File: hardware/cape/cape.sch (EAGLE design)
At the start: 156 parts, among them IC1 AD8422BRMZ, IC10 DAC8562_DGS_10, IC11 CAT24C256WI-GT3, IC12 LM27762DSSR, IC13 BQ25505, IC14 SN74LV4T125PWR, IC15 LMP7701MF, IC16 TXB0304RUTR, IC2 OPA2388DGK8_L, IC3 AD8422BRMZ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

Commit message: hardware: fixed wrong part number for constant supply LDO
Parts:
- IC8: value TPS73125DBVR -> TPS73101DBVR; device mylib:TPS73125DBVR -> shepherd:TPS73101DBVR
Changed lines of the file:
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@@
 <?xml version="1.0" encoding="utf-8"?>
 <!DOCTYPE eagle SYSTEM "eagle.dtd">
-<eagle version="9.3.2">
+<eagle version="9.4.2">
 <drawing>
 <settings>
@@
 <part name="C35" library="mylib" deviceset="C_SMD" device="0603" package3d_urn="urn:adsk.eagle:package:4925888/1" value="1u"/>
 <part name="R31" library="mylib" deviceset="R_SMD" device="0402" package3d_urn="urn:adsk.eagle:package:4924763/1" value="10k"/>
-<part name="IC8" library="mylib" deviceset="TPS73125DBVR" device=""/>
+<part name="IC8" library="shepherd" deviceset="TPS73101DBVR" device=""/>
 <part name="D2" library="mylib" deviceset="BAT43WS-HE3" device="SOD-323" package3d_urn="urn:adsk.eagle:package:6206822/1"/>
 <part name="R26" library="mylib" deviceset="R_SMD" device="0402" package3d_urn="urn:adsk.eagle:package:4924763/1" value="30k"/>

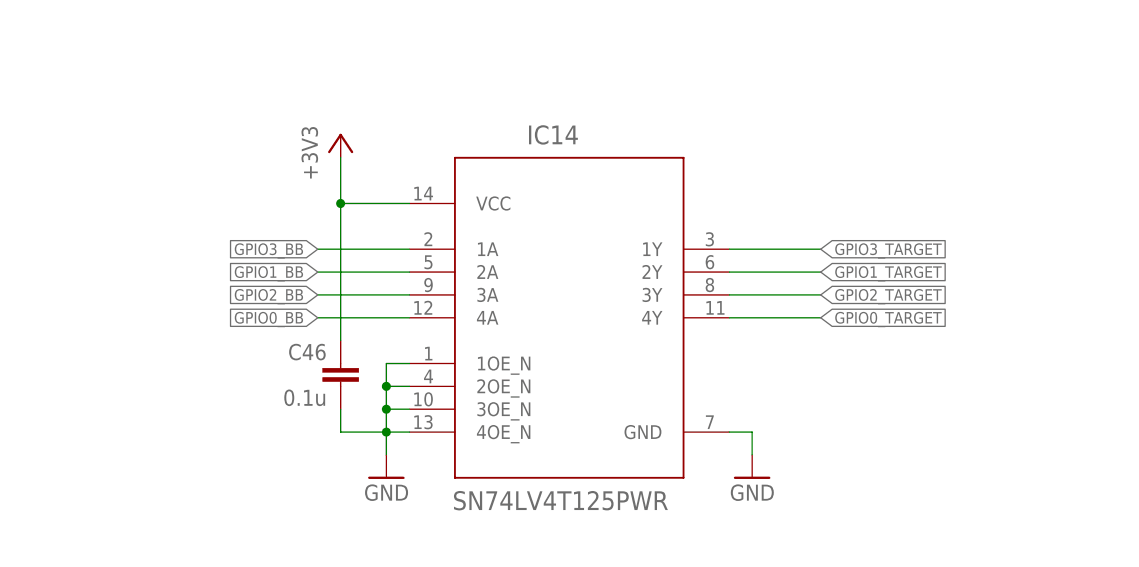
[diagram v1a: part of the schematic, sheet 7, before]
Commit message: hardware: fixed direction of level-converter
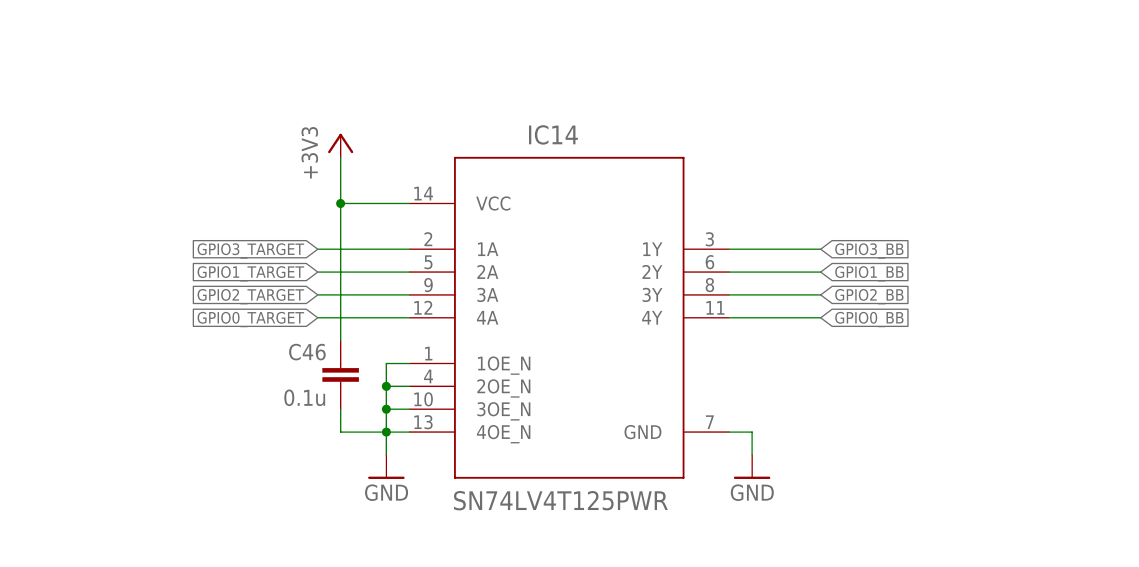
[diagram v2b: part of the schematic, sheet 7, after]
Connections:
- net GPIO0_BB: now also IC14.4Y; no longer IC14.4A
- net GPIO0_TARGET: now also IC14.4A; no longer IC14.4Y
- net GPIO1_BB: now also IC14.2Y; no longer IC14.2A
- net GPIO1_TARGET: now also IC14.2A; no longer IC14.2Y
- net GPIO2_BB: now also IC14.3Y; no longer IC14.3A
- net GPIO2_TARGET: now also IC14.3A; no longer IC14.3Y
- net GPIO3_BB: now also IC14.1Y; no longer IC14.1A
- net GPIO3_TARGET: now also IC14.1A; no longer IC14.1Y
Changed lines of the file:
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@@
 </segment>
 </net>
-<net name="GPIO3_BB" class="0">
+<net name="GPIO0_TARGET" class="0">
+<segment>
+<wire x1="53.34" y1="139.7" x2="43.18" y2="139.7" width="0.1524" layer="91"/>
+<label x="43.18" y="139.7" size="1.27" layer="95" rot="R180" xref="yes"/>
+<pinref part="IC14" gate="A" pin="4A"/>
+</segment>
+</net>
+<net name="GPIO1_TARGET" class="0">
+<segment>
+<wire x1="53.34" y1="144.78" x2="43.18" y2="144.78" width="0.1524" layer="91"/>
+<label x="43.18" y="144.78" size="1.27" layer="95" rot="R180" xref="yes"/>
+<pinref part="IC14" gate="A" pin="2A"/>
+</segment>
+</net>
+<net name="GPIO2_TARGET" class="0">
+<segment>
+<wire x1="53.34" y1="142.24" x2="43.18" y2="142.24" width="0.1524" layer="91"/>
+<label x="43.18" y="142.24" size="1.27" layer="95" rot="R180" xref="yes"/>
+<pinref part="IC14" gate="A" pin="3A"/>
+</segment>
+</net>
+<net name="GPIO3_TARGET" class="0">
 <segment>
 <wire x1="53.34" y1="147.32" x2="43.18" y2="147.32" width="0.1524" layer="91"/>
 <label x="43.18" y="147.32" size="1.27" layer="95" rot="R180" xref="yes"/>
 <pinref part="IC14" gate="A" pin="1A"/>
-</segment>
-</net>
-<net name="GPIO0_TARGET" class="0">
-<segment>
-<wire x1="88.9" y1="139.7" x2="99.06" y2="139.7" width="0.1524" layer="91"/>
-<label x="99.06" y="139.7" size="1.27" layer="95" xref="yes"/>
-<pinref part="IC14" gate="A" pin="4Y"/>
-</segment>
-</net>
-<net name="GPIO1_TARGET" class="0">
-<segment>
-<wire x1="88.9" y1="144.78" x2="99.06" y2="144.78" width="0.1524" layer="91"/>
-<label x="99.06" y="144.78" size="1.27" layer="95" xref="yes"/>
-<pinref part="IC14" gate="A" pin="2Y"/>
-</segment>
-</net>
-<net name="GPIO2_TARGET" class="0">
-<segment>
-<wire x1="88.9" y1="142.24" x2="99.06" y2="142.24" width="0.1524" layer="91"/>
-<label x="99.06" y="142.24" size="1.27" layer="95" xref="yes"/>
-<pinref part="IC14" gate="A" pin="3Y"/>
-</segment>
-</net>
-<net name="GPIO3_TARGET" class="0">
-<segment>
-<wire x1="88.9" y1="147.32" x2="99.06" y2="147.32" width="0.1524" layer="91"/>
-<label x="99.06" y="147.32" size="1.27" layer="95" xref="yes"/>
-<pinref part="IC14" gate="A" pin="1Y"/>
 </segment>
 </net>
@@
 <wire x1="86.36" y1="50.8" x2="104.14" y2="50.8" width="0.1524" layer="91"/>
 <junction x="104.14" y="50.8"/>
-</segment>
-</net>
-<net name="GPIO2_BB" class="0">
-<segment>
-<wire x1="53.34" y1="142.24" x2="43.18" y2="142.24" width="0.1524" layer="91"/>
-<label x="43.18" y="142.24" size="1.27" layer="95" rot="R180" xref="yes"/>
-<pinref part="IC14" gate="A" pin="3A"/>
 </segment>
 </net>
@@
 </segment>
 </net>
-<net name="GPIO0_BB" class="0">
+<net name="GPIO3_BB" class="0">
 <segment>
-<wire x1="53.34" y1="139.7" x2="43.18" y2="139.7" width="0.1524" layer="91"/>
-<label x="43.18" y="139.7" size="1.27" layer="95" rot="R180" xref="yes"/>
-<pinref part="IC14" gate="A" pin="4A"/>
+<wire x1="88.9" y1="147.32" x2="99.06" y2="147.32" width="0.1524" layer="91"/>
+<label x="99.06" y="147.32" size="1.27" layer="95" xref="yes"/>
+<pinref part="IC14" gate="A" pin="1Y"/>
 </segment>
 </net>
 <net name="GPIO1_BB" class="0">
 <segment>
-<wire x1="53.34" y1="144.78" x2="43.18" y2="144.78" width="0.1524" layer="91"/>
-<label x="43.18" y="144.78" size="1.27" layer="95" rot="R180" xref="yes"/>
-<pinref part="IC14" gate="A" pin="2A"/>
+<wire x1="88.9" y1="144.78" x2="99.06" y2="144.78" width="0.1524" layer="91"/>
+<label x="99.06" y="144.78" size="1.27" layer="95" xref="yes"/>
+<pinref part="IC14" gate="A" pin="2Y"/>
 </segment>
 </net>
+<net name="GPIO2_BB" class="0">
+<segment>
+<wire x1="88.9" y1="142.24" x2="99.06" y2="142.24" width="0.1524" layer="91"/>
+<label x="99.06" y="142.24" size="1.27" layer="95" xref="yes"/>
+<pinref part="IC14" gate="A" pin="3Y"/>
+</segment>
+</net>
+<net name="GPIO0_BB" class="0">
+<segment>
+<wire x1="88.9" y1="139.7" x2="99.06" y2="139.7" width="0.1524" layer="91"/>
+<label x="99.06" y="139.7" size="1.27" layer="95" xref="yes"/>
+<pinref part="IC14" gate="A" pin="4Y"/>
+</segment>
+</net>

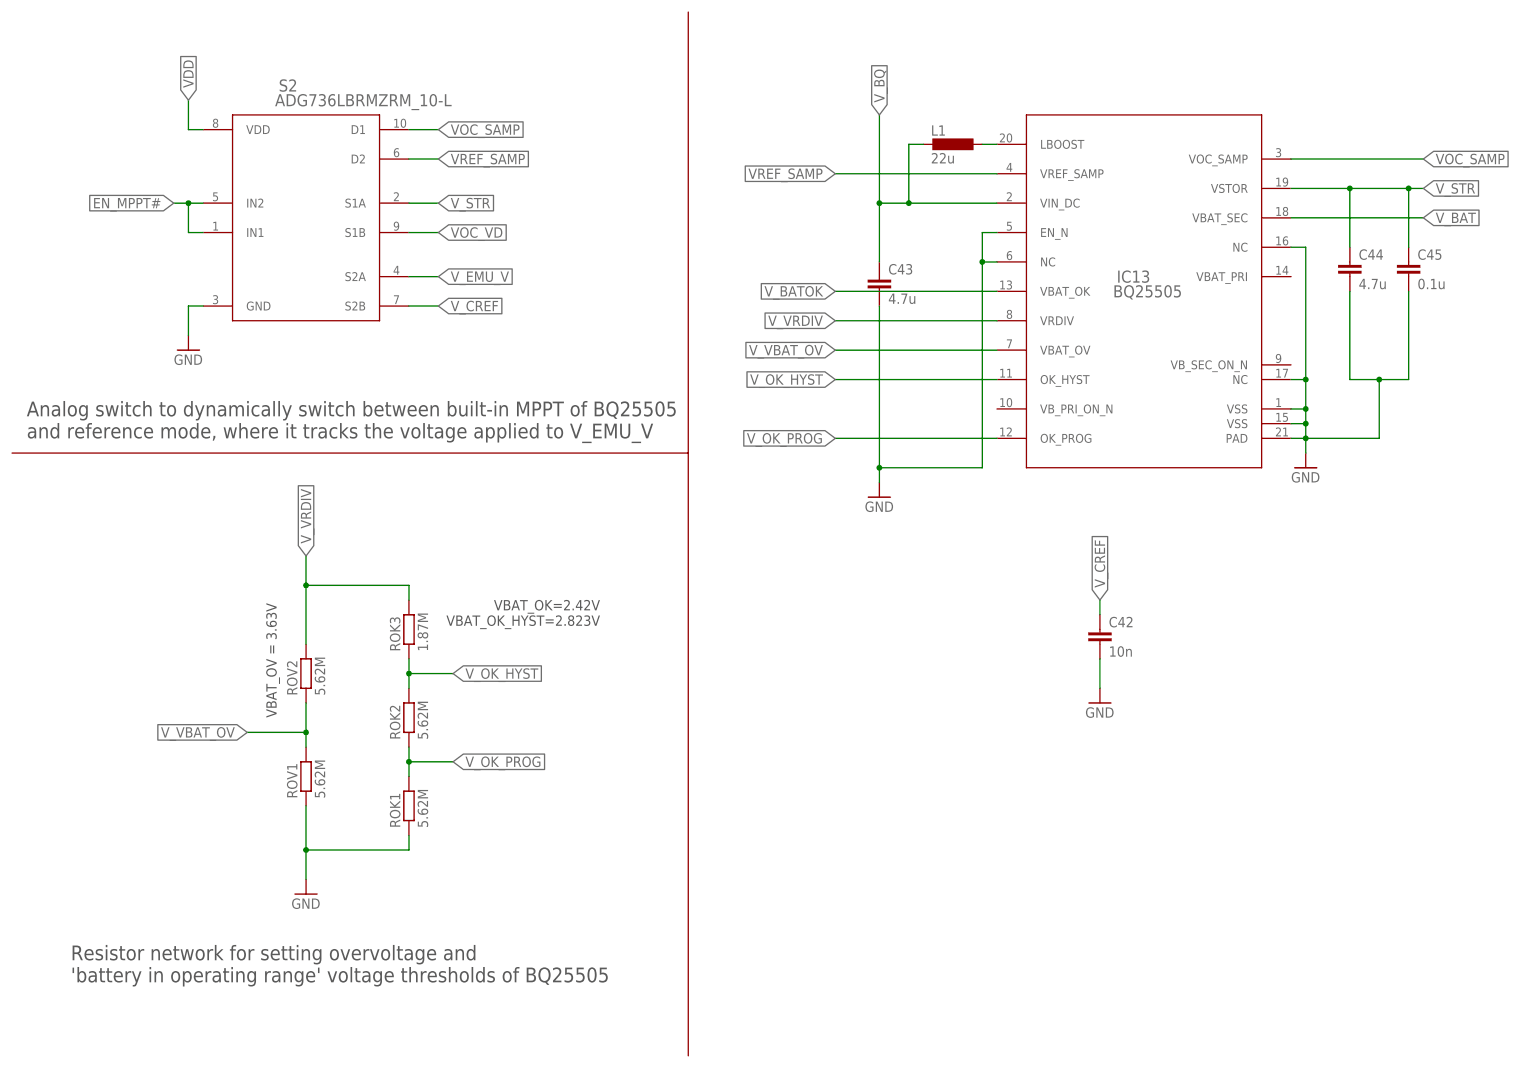
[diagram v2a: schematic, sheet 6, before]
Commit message: hardware: cape: reverted to BQ25504, fixed booting bug and added logo
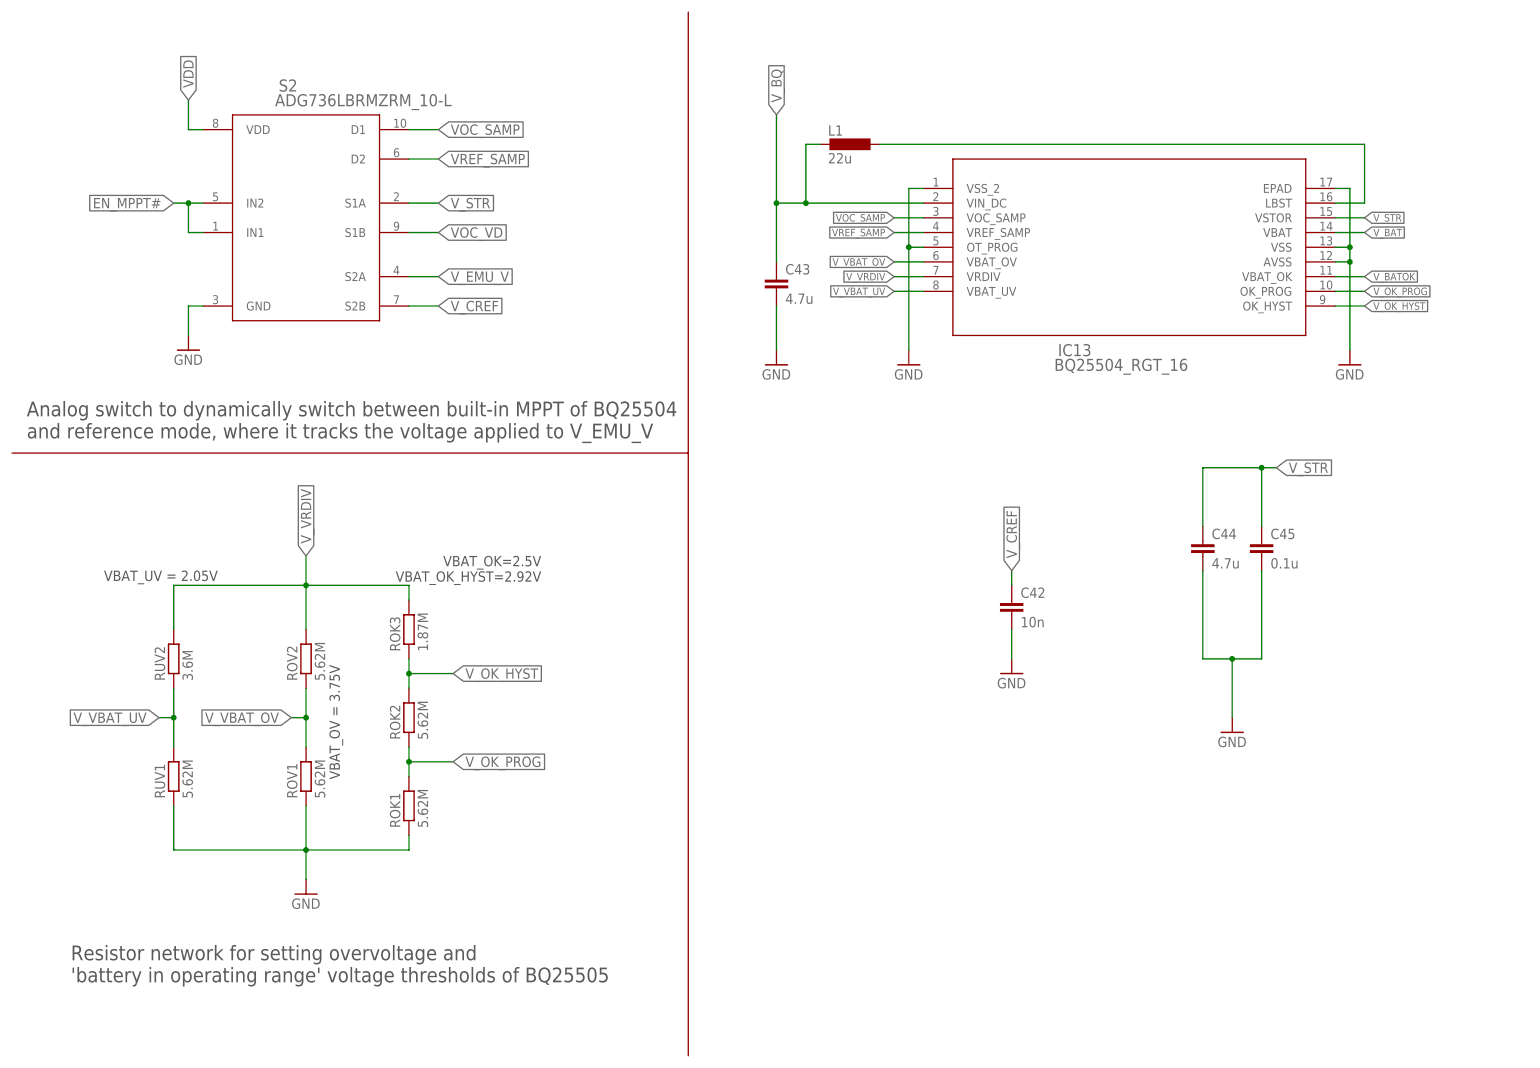
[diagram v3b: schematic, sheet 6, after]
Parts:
- added D4, D5, D6, D7: ACDBQC0130L-HF0402, shepherd:ACDBQC0130L-HF0402
- added RUV1: 5.62M, mylib:R_SMD0603
- added RUV2: 3.6M, mylib:R_SMD0603
- IC13: value BQ25505 -> BQ25504_RGT_16; device mylib:BQ25505 -> shepherd:BQ25504_RGT_16
- ROK1, ROK2, ROK3, ROV1, ROV2: device mylib:R_SMD0805 -> mylib:R_SMD0603
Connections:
- new net N$43: D4.A, IC14.1Y
- new net N$47: D5.A, IC14.2Y
- new net N$50: D6.A, IC14.3Y
- new net N$51: D7.A, IC14.4Y
- new net V_VBAT_UV: IC13.VBAT_UV, RUV1.2, RUV2.1
- net GND: now also IC13.AVSS, IC13.EPAD, IC13.OT_PROG, IC13.VSS, IC13.VSS_2, RUV1.1; no longer IC13.EN_N, IC13.NC@1, IC13.NC@2, IC13.NC@3, IC13.PAD, IC13.VSS@1, IC13.VSS@2
- net GPIO0_BB: now also D7.C; no longer IC14.4Y
- net GPIO1_BB: now also D5.C; no longer IC14.2Y
- net GPIO2_BB: now also D6.C; no longer IC14.3Y
- net GPIO3_BB: now also D4.C; no longer IC14.1Y
- net N$19: now also IC13.LBST; no longer IC13.LBOOST
- net V_BAT: now also IC13.VBAT; no longer IC13.VBAT_SEC
- net V_VRDIV: now also RUV2.2
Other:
- note added: "Analog switch to dynamically switch between built-in MPPT of BQ25504 and reference mode, where it tracks the voltage applied to V_EMU_V"
- note added: "VBAT_OK=2.5V VBAT_OK_HYST=2.92V"
- note added: "VBAT_OV = 3.75V"
- note added: "VBAT_UV = 2.05V"
- note removed: "Analog switch to dynamically switch between built-in MPPT of BQ25505 and reference mode, where it tracks the voltage applied to V_EMU_V"
- note removed: "VBAT_OK=2.42V VBAT_OK_HYST=2.823V"
- note removed: "VBAT_OV = 3.63V"
- moved on the sheet: C42, C43, C44, C45, C46, IC14, L1, ROV2
